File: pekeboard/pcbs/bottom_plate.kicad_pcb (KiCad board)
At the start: 2 copper layers, 148.2 x 123.9 mm, 0 parts

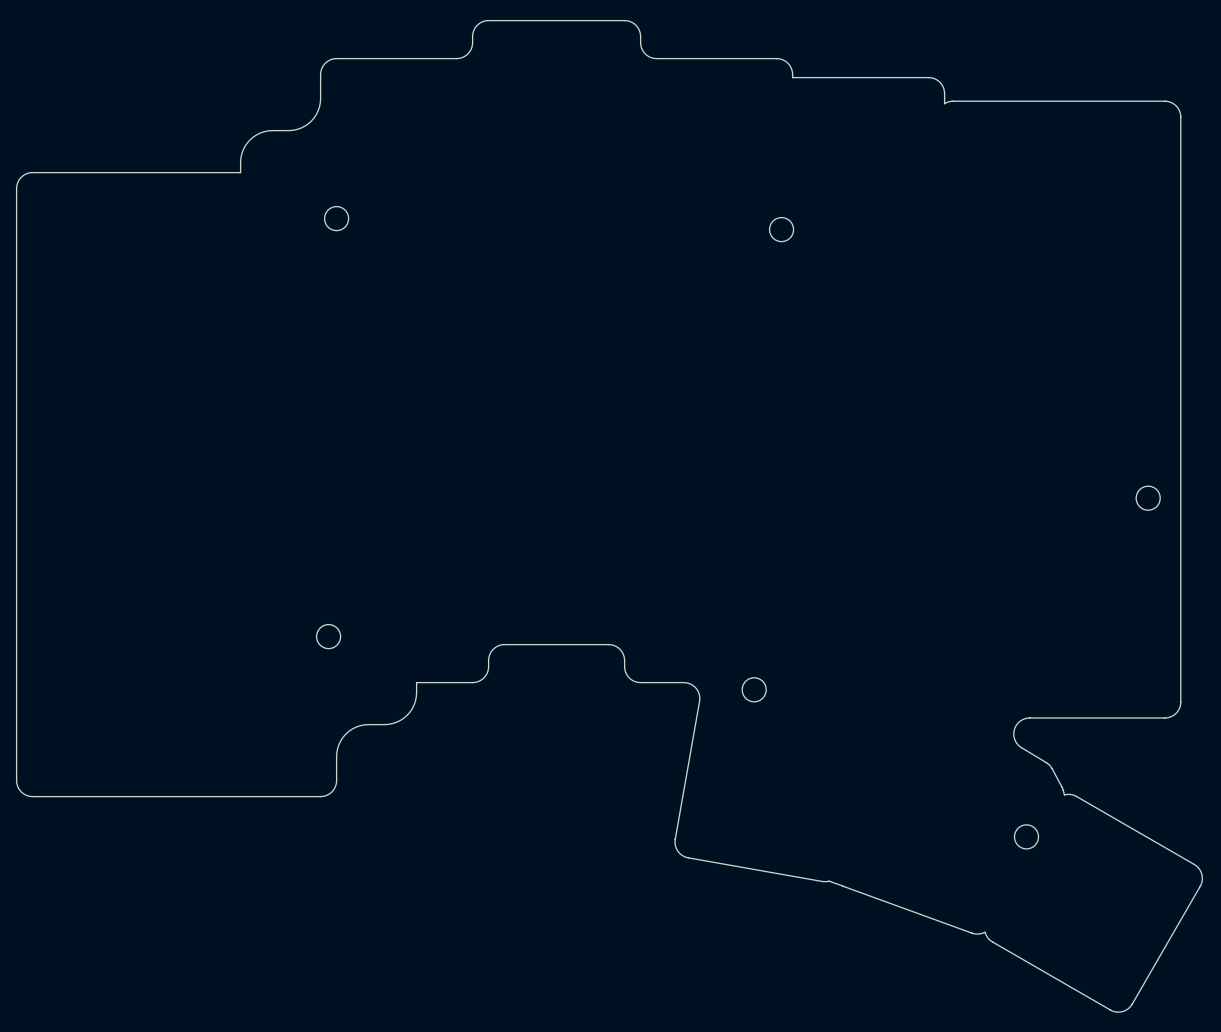
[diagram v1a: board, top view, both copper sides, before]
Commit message: Removing right side for Cases section
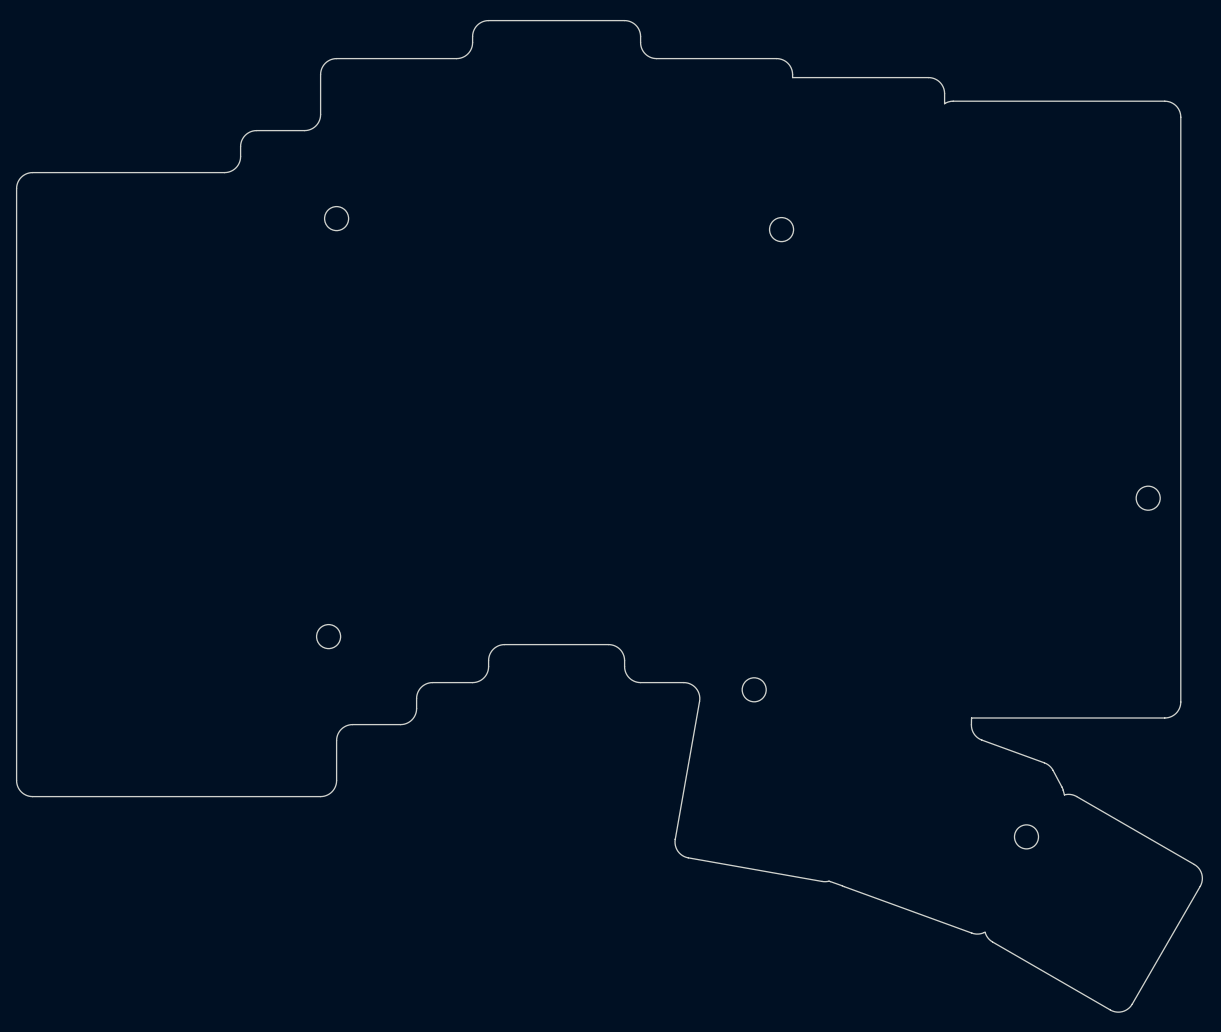
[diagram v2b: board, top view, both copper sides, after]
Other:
- outline, holes or cut-outs redrawn

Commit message: V1.0 Fabrication sent to JLCPCB
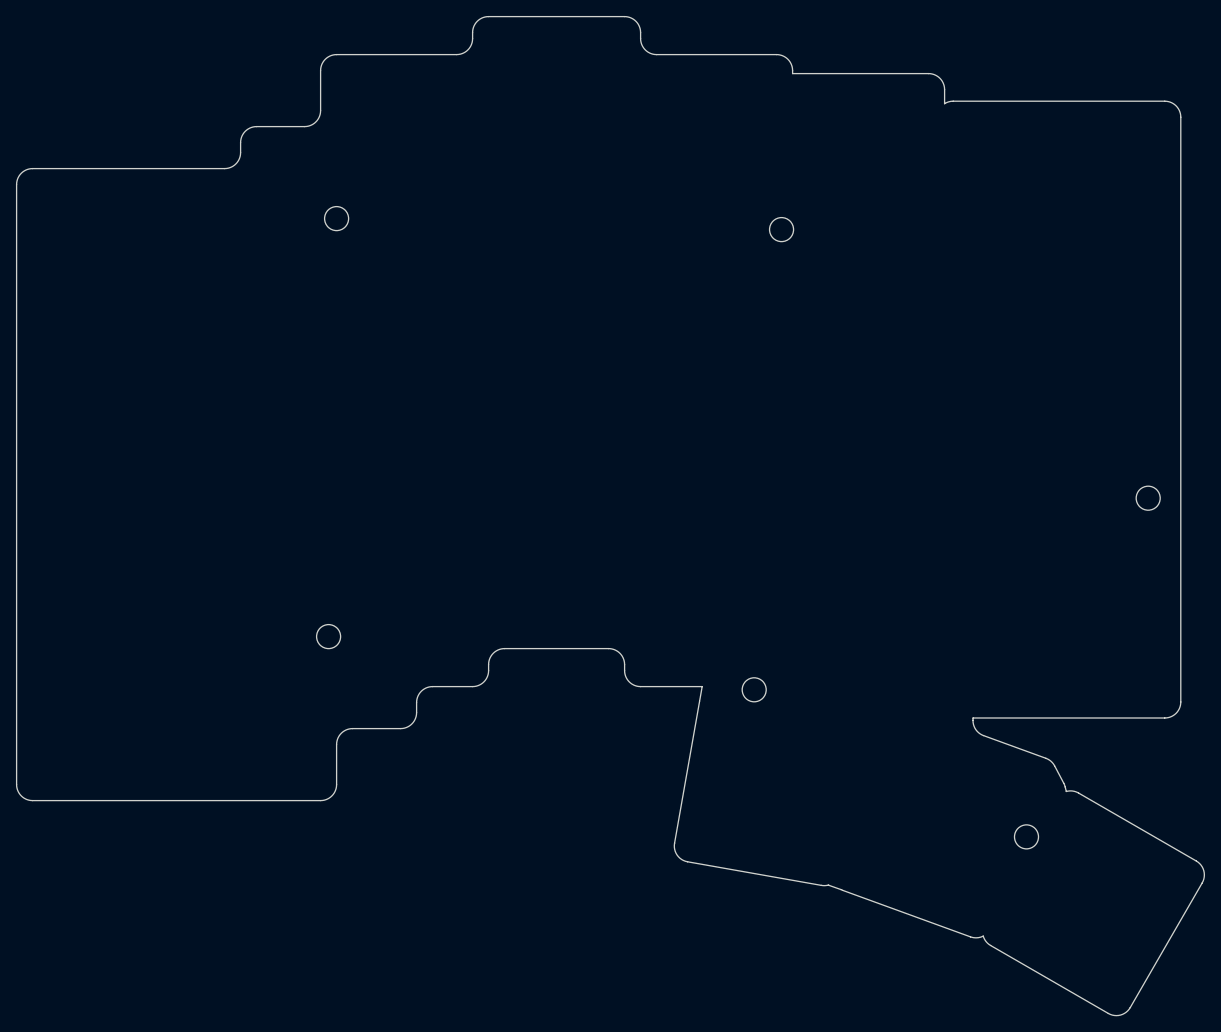
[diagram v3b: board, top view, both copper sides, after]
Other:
- board size 148.2 x 123.9 mm -> 148.5 x 124.9 mm
